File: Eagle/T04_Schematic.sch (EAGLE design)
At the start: 25 parts, among them Y1 16 MHz

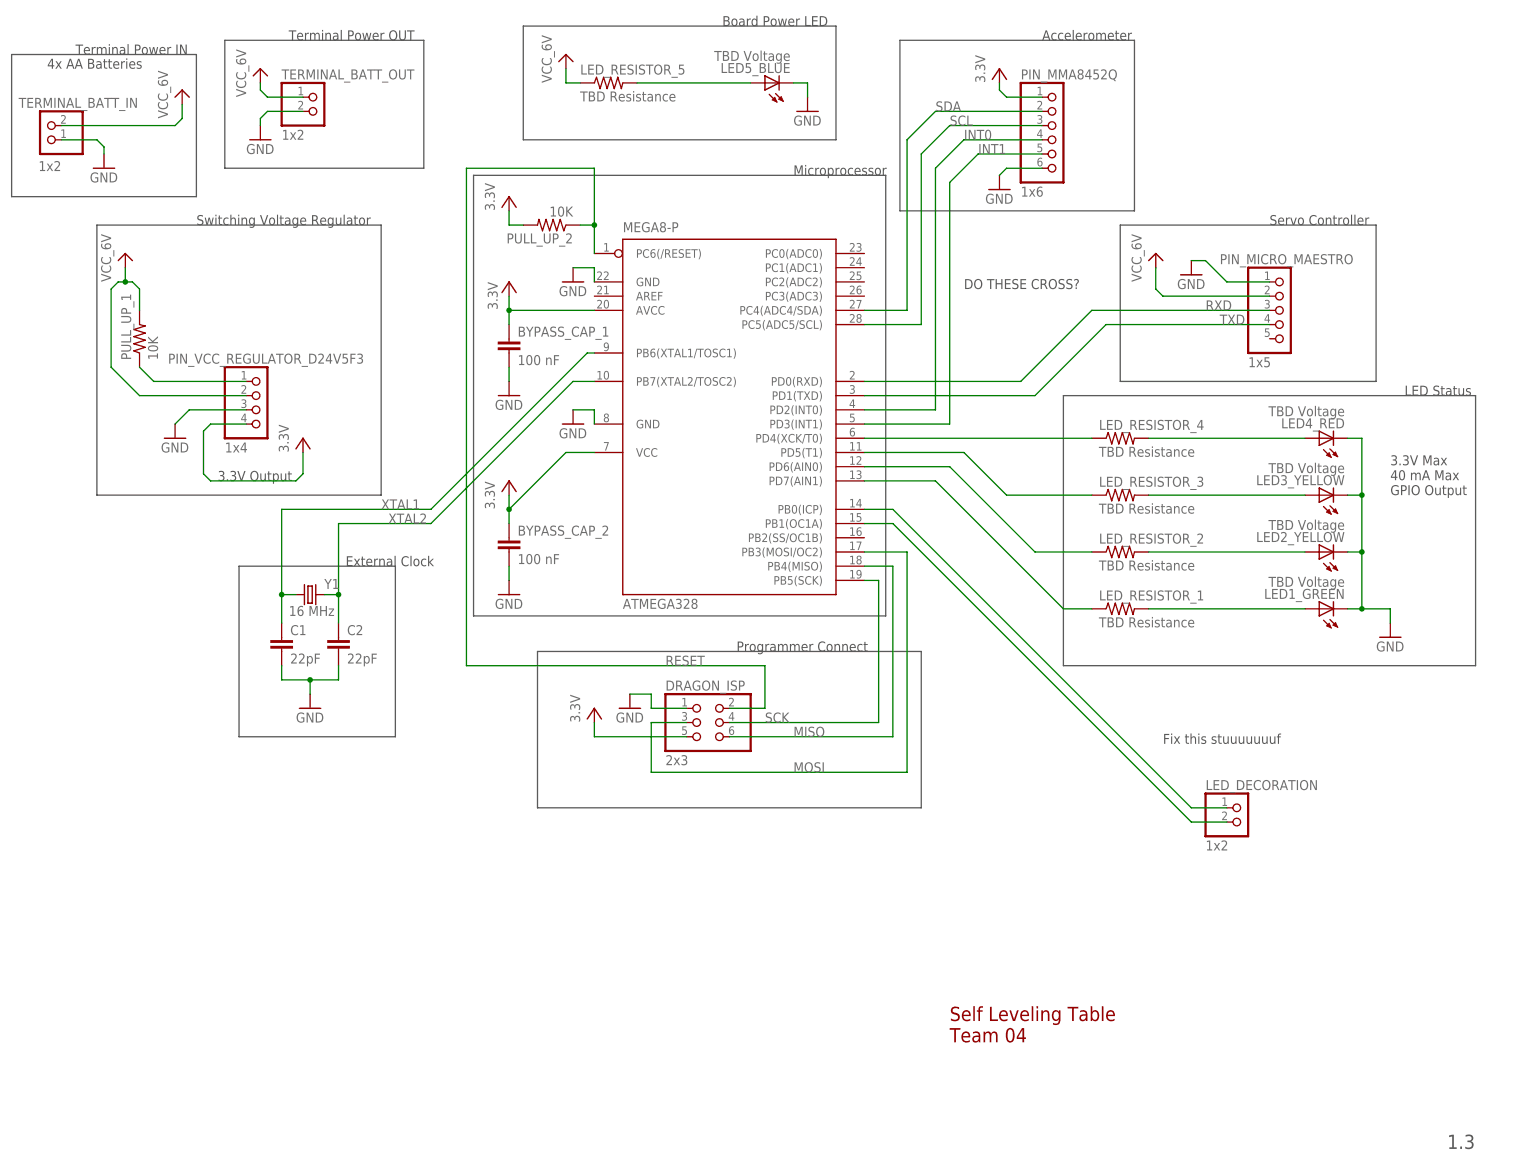
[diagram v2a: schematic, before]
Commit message: Schematic and Layout
Added DRC passing PCB layout.
Updated Schematic, added buffer for 5V LED control.
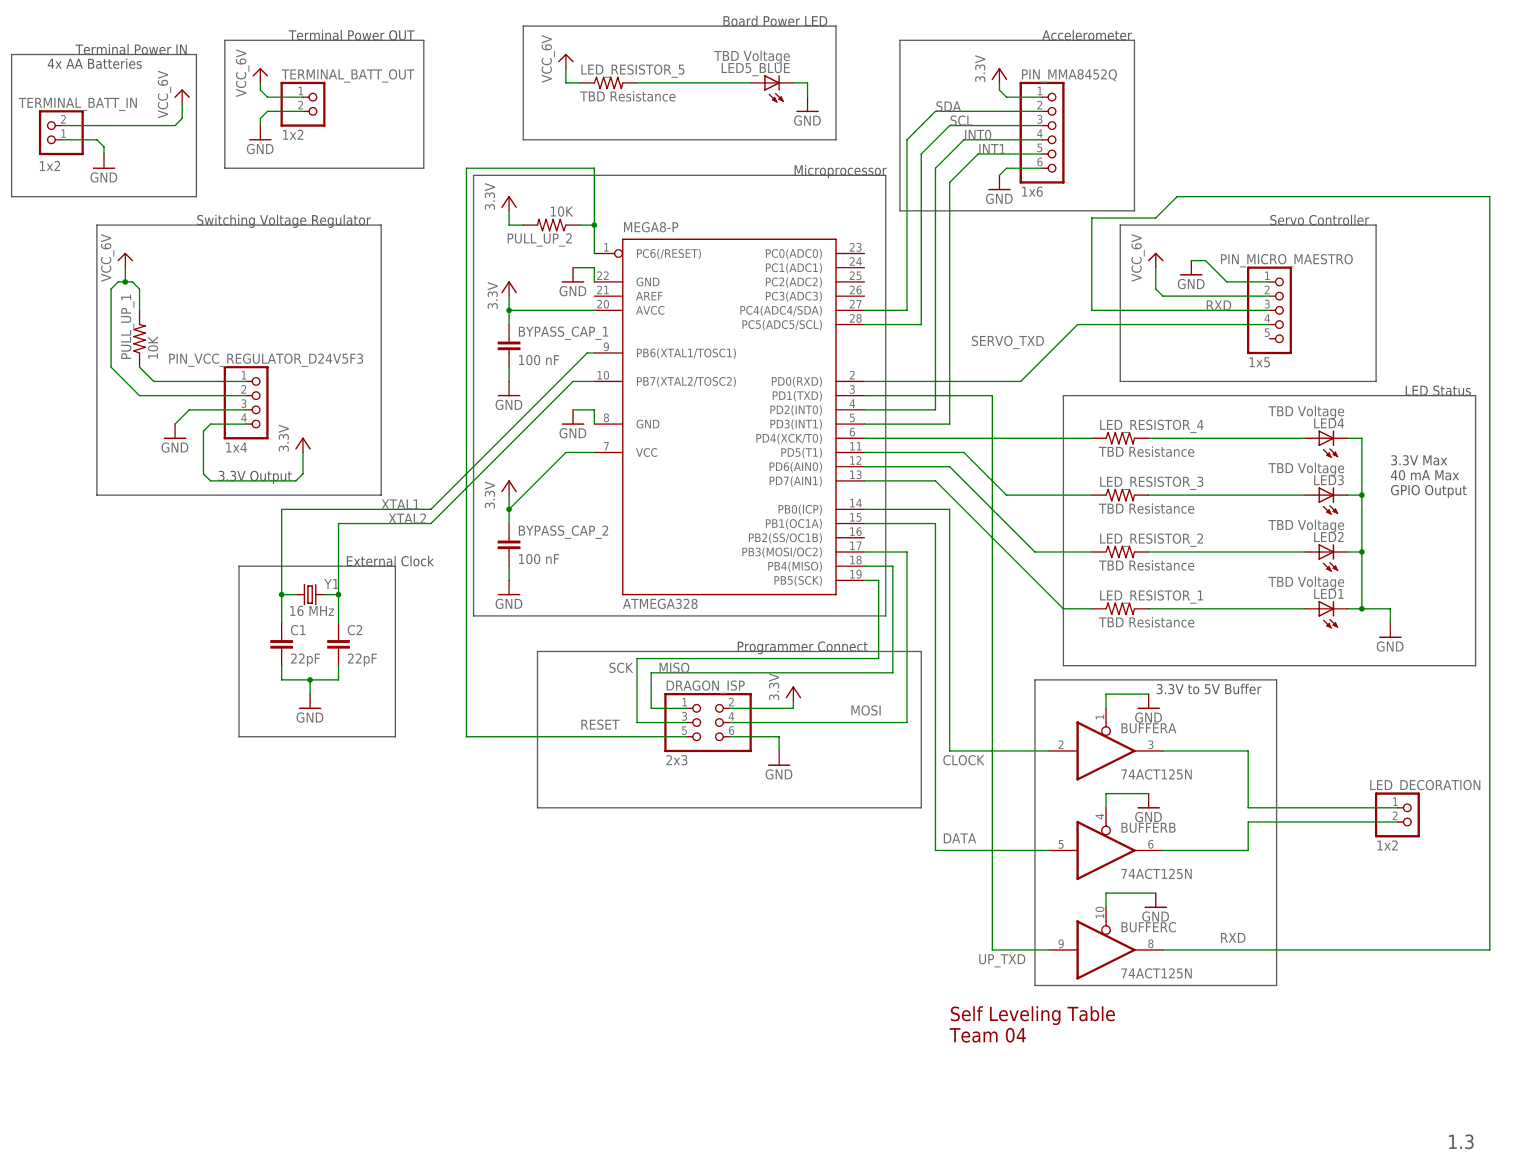
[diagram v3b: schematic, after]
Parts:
- added BUFFER: 74ACT125N, 74xx-eu:74ACT125N
- renumbered LED1_GREEN to LED1, LED2_YELLOW to LED2, LED3_YELLOW to LED3, LED4_RED to LED4
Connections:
- removed net N$7: ATMEGA328.PB1(OC1A), LED_DECORATION.2
- removed net TXD: ATMEGA328.PD1(TXD), PIN_MICRO_MAESTRO.4
- new net DATA: ATMEGA328.PB1(OC1A), BUFFERB.I
- new net N$13: BUFFERB.O, LED_DECORATION.2
- new net N$8: BUFFERA.O, LED_DECORATION.1
- new net SERVO_TXD: ATMEGA328.PD0(RXD), PIN_MICRO_MAESTRO.4
- new net UP_TXD: ATMEGA328.PD1(TXD), BUFFERC.I
- net CLOCK: now also BUFFERA.I; no longer LED_DECORATION.1
- net GND: now also BUFFERA.OE, BUFFERB.OE, BUFFERC.OE, DRAGON_ISP.6; no longer DRAGON_ISP.1
- net MISO: now also DRAGON_ISP.1; no longer DRAGON_ISP.6
- net MOSI: now also DRAGON_ISP.4; no longer DRAGON_ISP.3
- net RESET: now also DRAGON_ISP.5; no longer DRAGON_ISP.2
- net RXD: now also BUFFERC.O; no longer ATMEGA328.PD0(RXD)
- net SCK: now also DRAGON_ISP.3; no longer DRAGON_ISP.4
- net VCC: now also DRAGON_ISP.2; no longer DRAGON_ISP.5
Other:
- note added: "3.3V to 5V Buffer"
- note removed: "DO THESE CROSS?"
- note removed: "Fix this stuuuuuuuf"
- moved on the sheet: LED_DECORATION

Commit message: DRC Error Free Layout + Schematic Update
Made changes to layout based on feedback from class.
Added linear regulator to schematic for 5V supply.
Will need group review.
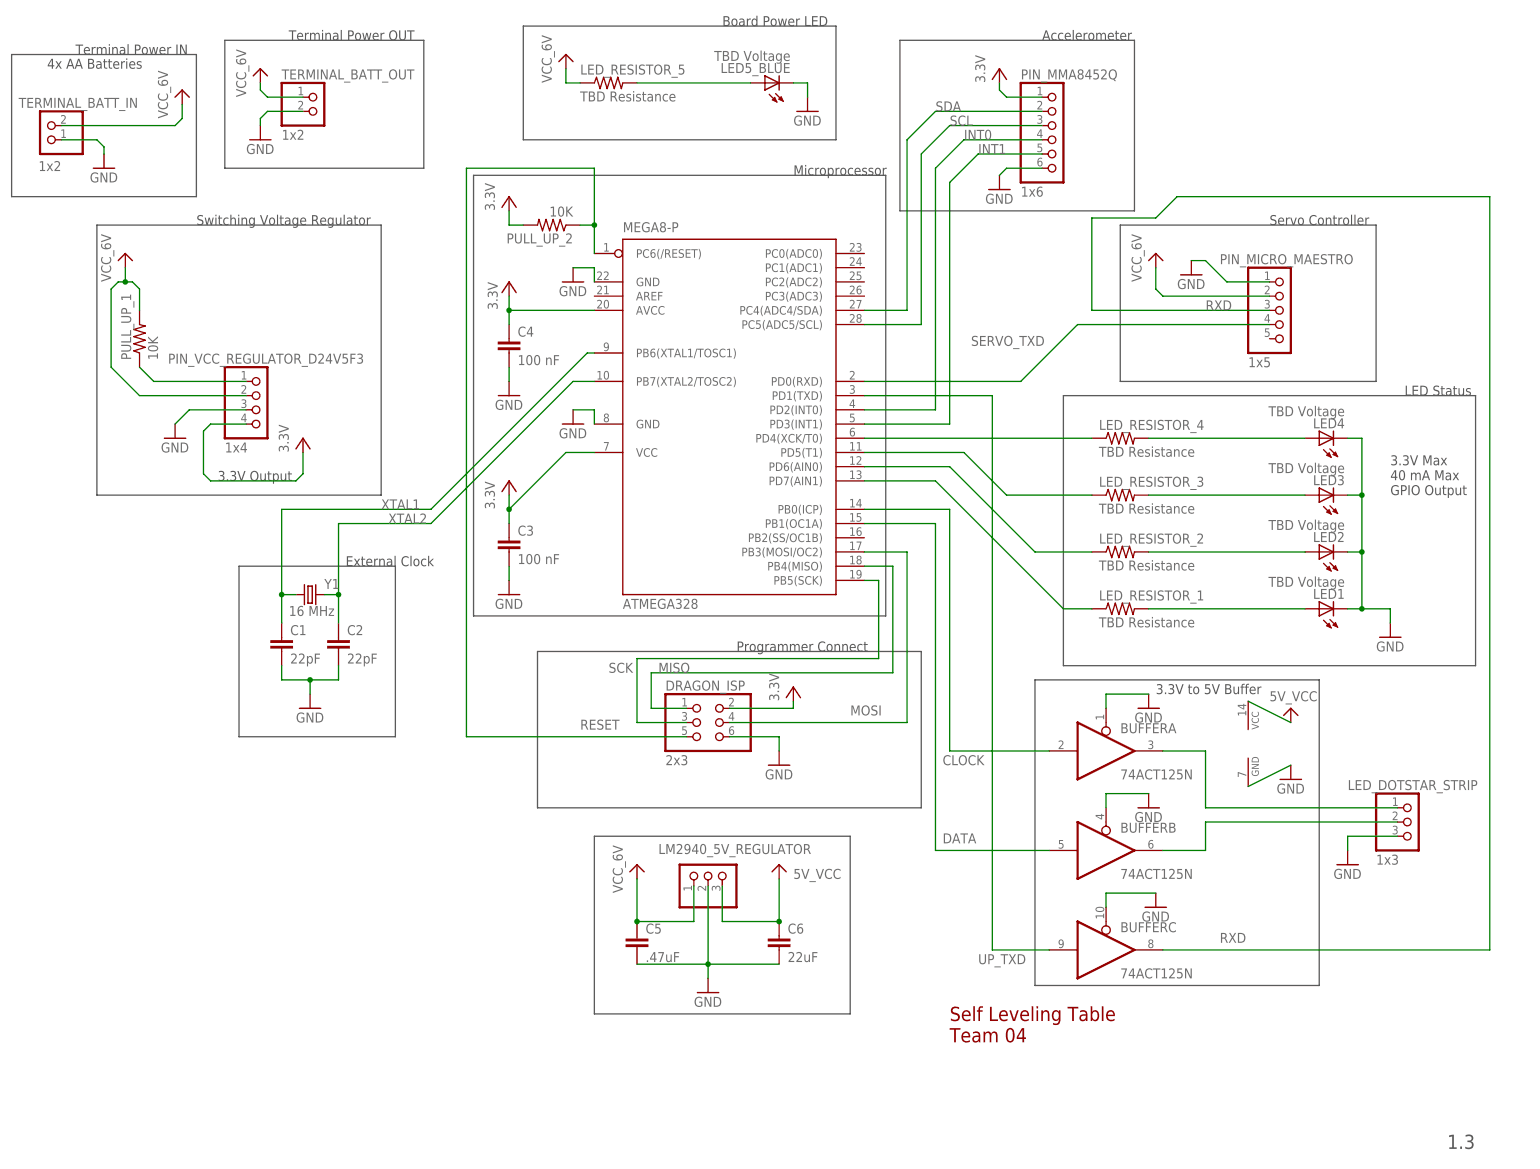
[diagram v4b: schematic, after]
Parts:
- removed LED_DECORATION: 1x2, pinhead:PINHD-1X2
- added C5: .47uF, rcl:C-EUC1206
- added C6: 22uF, rcl:C-EUC1206
- added LED_DOTSTAR_STRIP: 1x3, pinhead:PINHD-1X3
- added LM2940_5V_REGULATOR: (no value), pinhead:PINHD-1X3
- renumbered BYPASS_CAP_1 to C4, BYPASS_CAP_2 to C3
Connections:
- new net 5V_VCC: BUFFERP.VCC, C6.1, LM2940_5V_REGULATOR.3
- net GND: now also BUFFERP.GND, C5.2, C6.2, LED_DOTSTAR_STRIP.3, LM2940_5V_REGULATOR.2
- net N$13: now also LED_DOTSTAR_STRIP.2; no longer LED_DECORATION.2
- net N$8: now also LED_DOTSTAR_STRIP.1; no longer LED_DECORATION.1
- net VCC_6V: now also C5.1, LM2940_5V_REGULATOR.1

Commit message: Final(?) Layout
Increase board size for more room to solder.
Improved power signal layout.
Added missing GND and VCC to Dotstar LEDs.
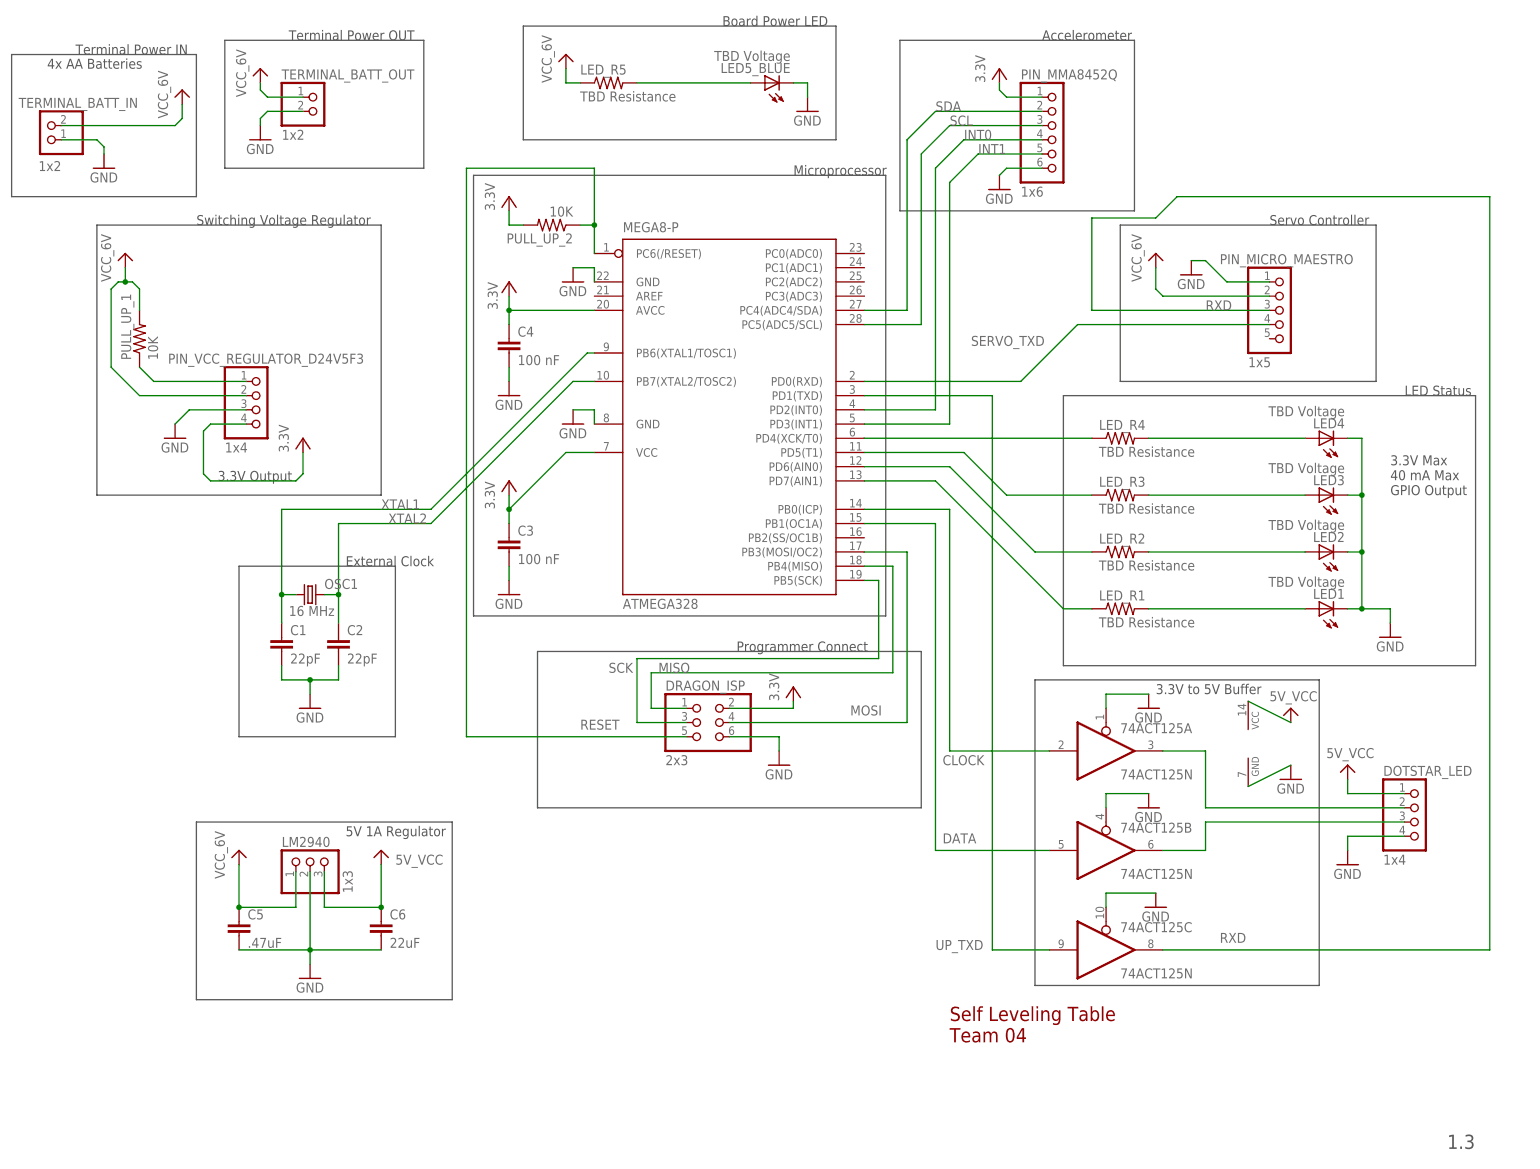
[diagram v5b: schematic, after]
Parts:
- removed LED_DOTSTAR_STRIP: 1x3, pinhead:PINHD-1X3
- removed LM2940_5V_REGULATOR: (no value), pinhead:PINHD-1X3
- added DOTSTAR_LED: 1x4, pinhead:PINHD-1X4
- added LM2940: 1x3, pinhead:PINHD-1X3
- renumbered BUFFER to 74ACT125, LED_RESISTOR_1 to LED_R1, LED_RESISTOR_2 to LED_R2, LED_RESISTOR_3 to LED_R3, LED_RESISTOR_4 to LED_R4, LED_RESISTOR_5 to LED_R5, Y1 to OSC1
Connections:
- net 5V_VCC: now also DOTSTAR_LED.1, LM2940.3; no longer LM2940_5V_REGULATOR.3
- net GND: now also DOTSTAR_LED.4, LM2940.2; no longer LED_DOTSTAR_STRIP.3, LM2940_5V_REGULATOR.2
- net N$13: now also DOTSTAR_LED.3; no longer LED_DOTSTAR_STRIP.2
- net N$8: now also DOTSTAR_LED.2; no longer LED_DOTSTAR_STRIP.1
- net VCC_6V: now also LM2940.1; no longer LM2940_5V_REGULATOR.1
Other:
- note added: "5V 1A Regulator"
- moved on the sheet: C5, C6

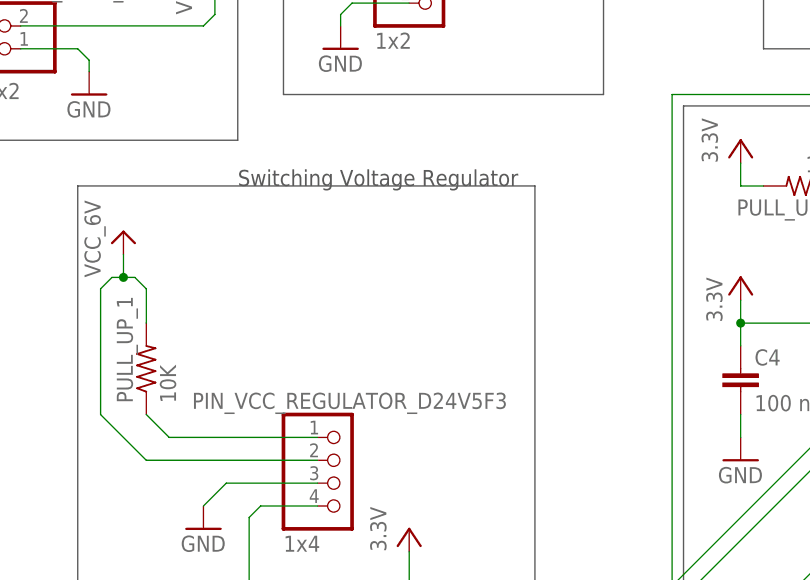
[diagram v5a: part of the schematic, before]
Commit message: Fixed Typo in Component Name
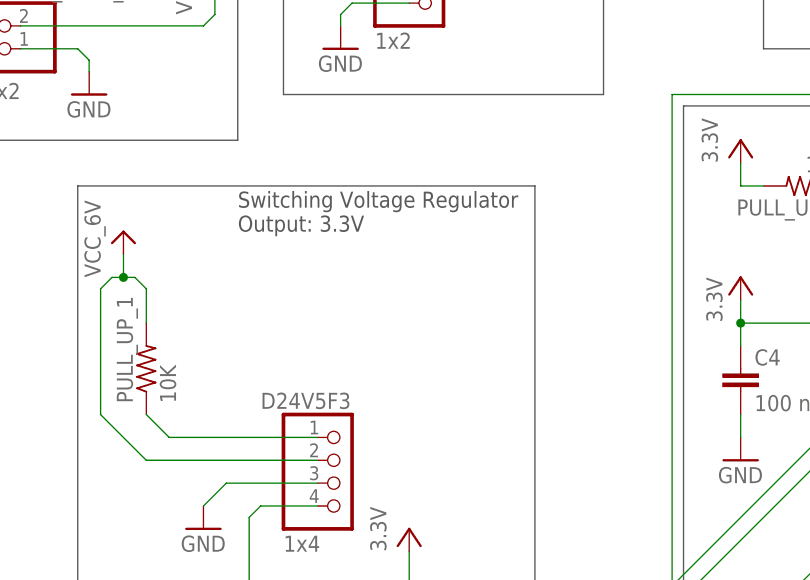
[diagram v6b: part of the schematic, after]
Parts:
- renumbered PIN_VCC_REGULATOR_D24V5F3 to D24V5F3
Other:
- note added: "Switching Voltage Regulator Output: 3.3V"
- note removed: "Switching Voltage Regulator"
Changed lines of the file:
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@@
 <setting verticaltext="up"/>
 </settings>
-<grid distance="0.05" unitdist="inch" unit="inch" style="lines" multiple="2" display="yes" altdistance="0.01" altunitdist="inch" altunit="inch"/>
+<grid distance="0.1" unitdist="inch" unit="inch" style="lines" multiple="1" display="no" altdistance="0.01" altunitdist="inch" altunit="inch"/>
 <layers>
 <layer number="1" name="Top" color="4" fill="1" visible="no" active="no"/>
@@
 <part name="PIN_MMA8452Q" library="pinhead" deviceset="PINHD-1X6" device="" value="1x6"/>
 <part name="PIN_MICRO_MAESTRO" library="pinhead" deviceset="PINHD-1X5" device="" value="1x5"/>
-<part name="PIN_VCC_REGULATOR_D24V5F3" library="pinhead" deviceset="PINHD-1X4" device="" value="1x4"/>
+<part name="D24V5F3" library="pinhead" deviceset="PINHD-1X4" device="" value="1x4"/>
 <part name="TERMINAL_BATT_IN" library="pinhead" deviceset="PINHD-1X2" device="" value="1x2"/>
 <part name="TERMINAL_BATT_OUT" library="pinhead" deviceset="PINHD-1X2" device="" value="1x2"/>
@@
 <text x="6.35" y="152.4" size="1.778" layer="97">Terminal Power IN</text>
 <text x="44.45" y="154.94" size="1.778" layer="97">Terminal Power OUT</text>
-<text x="27.94" y="121.92" size="1.778" layer="97">Switching Voltage Regulator</text>
+<text x="27.94" y="116.84" size="1.778" layer="97">Switching Voltage Regulator
+Output: 3.3V</text>
 <text x="162.56" y="-24.13" size="2.54" layer="94">Self Leveling Table
 Team 04</text>
@@
 <attribute name="VALUE" x="215.9" y="96.52" size="1.778" layer="96"/>
 </instance>
-<instance part="PIN_VCC_REGULATOR_D24V5F3" gate="A" x="39.37" y="88.9" smashed="yes">
-<attribute name="NAME" x="22.86" y="97.155" size="1.778" layer="95"/>
+<instance part="D24V5F3" gate="A" x="39.37" y="88.9" smashed="yes">
+<attribute name="NAME" x="30.48" y="97.155" size="1.778" layer="95"/>
 <attribute name="VALUE" x="33.02" y="81.28" size="1.778" layer="96"/>
 </instance>
@@
 </segment>
 <segment>
-<pinref part="PIN_VCC_REGULATOR_D24V5F3" gate="A" pin="3"/>
+<pinref part="D24V5F3" gate="A" pin="3"/>
 <pinref part="GND5" gate="1" pin="GND"/>
 <wire x1="36.83" y1="88.9" x2="26.67" y2="88.9" width="0.1524" layer="91"/>
@@
 <segment>
 <pinref part="P+1" gate="VCC" pin="VCC"/>
-<pinref part="PIN_VCC_REGULATOR_D24V5F3" gate="A" pin="4"/>
+<pinref part="D24V5F3" gate="A" pin="4"/>
 <wire x1="46.99" y1="77.47" x2="46.99" y2="81.28" width="0.1524" layer="91"/>
 <wire x1="36.83" y1="86.36" x2="30.48" y2="86.36" width="0.1524" layer="91"/>
@@
 <net name="V_REG_RESET" class="0">
 <segment>
-<pinref part="PIN_VCC_REGULATOR_D24V5F3" gate="A" pin="1"/>
+<pinref part="D24V5F3" gate="A" pin="1"/>
 <pinref part="PULL_UP_1" gate="G$1" pin="1"/>
 <wire x1="36.83" y1="93.98" x2="20.32" y2="93.98" width="0.1524" layer="91"/>
@@
 </segment>
 <segment>
-<pinref part="PIN_VCC_REGULATOR_D24V5F3" gate="A" pin="2"/>
+<pinref part="D24V5F3" gate="A" pin="2"/>
 <wire x1="36.83" y1="91.44" x2="17.78" y2="91.44" width="0.1524" layer="91"/>
 <wire x1="17.78" y1="91.44" x2="12.7" y2="96.52" width="0.1524" layer="91"/>
